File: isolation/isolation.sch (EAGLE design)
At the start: 37 parts, among them IC1 XTLV61048DBVR, IC2 SN74HC14DRG3, IC3 SN74HCS32PWR, IC4 SN74HCS08DYYR, J1 S4B-XH-A_LF__SN_, J2 S4B-XH-A_LF__SN_

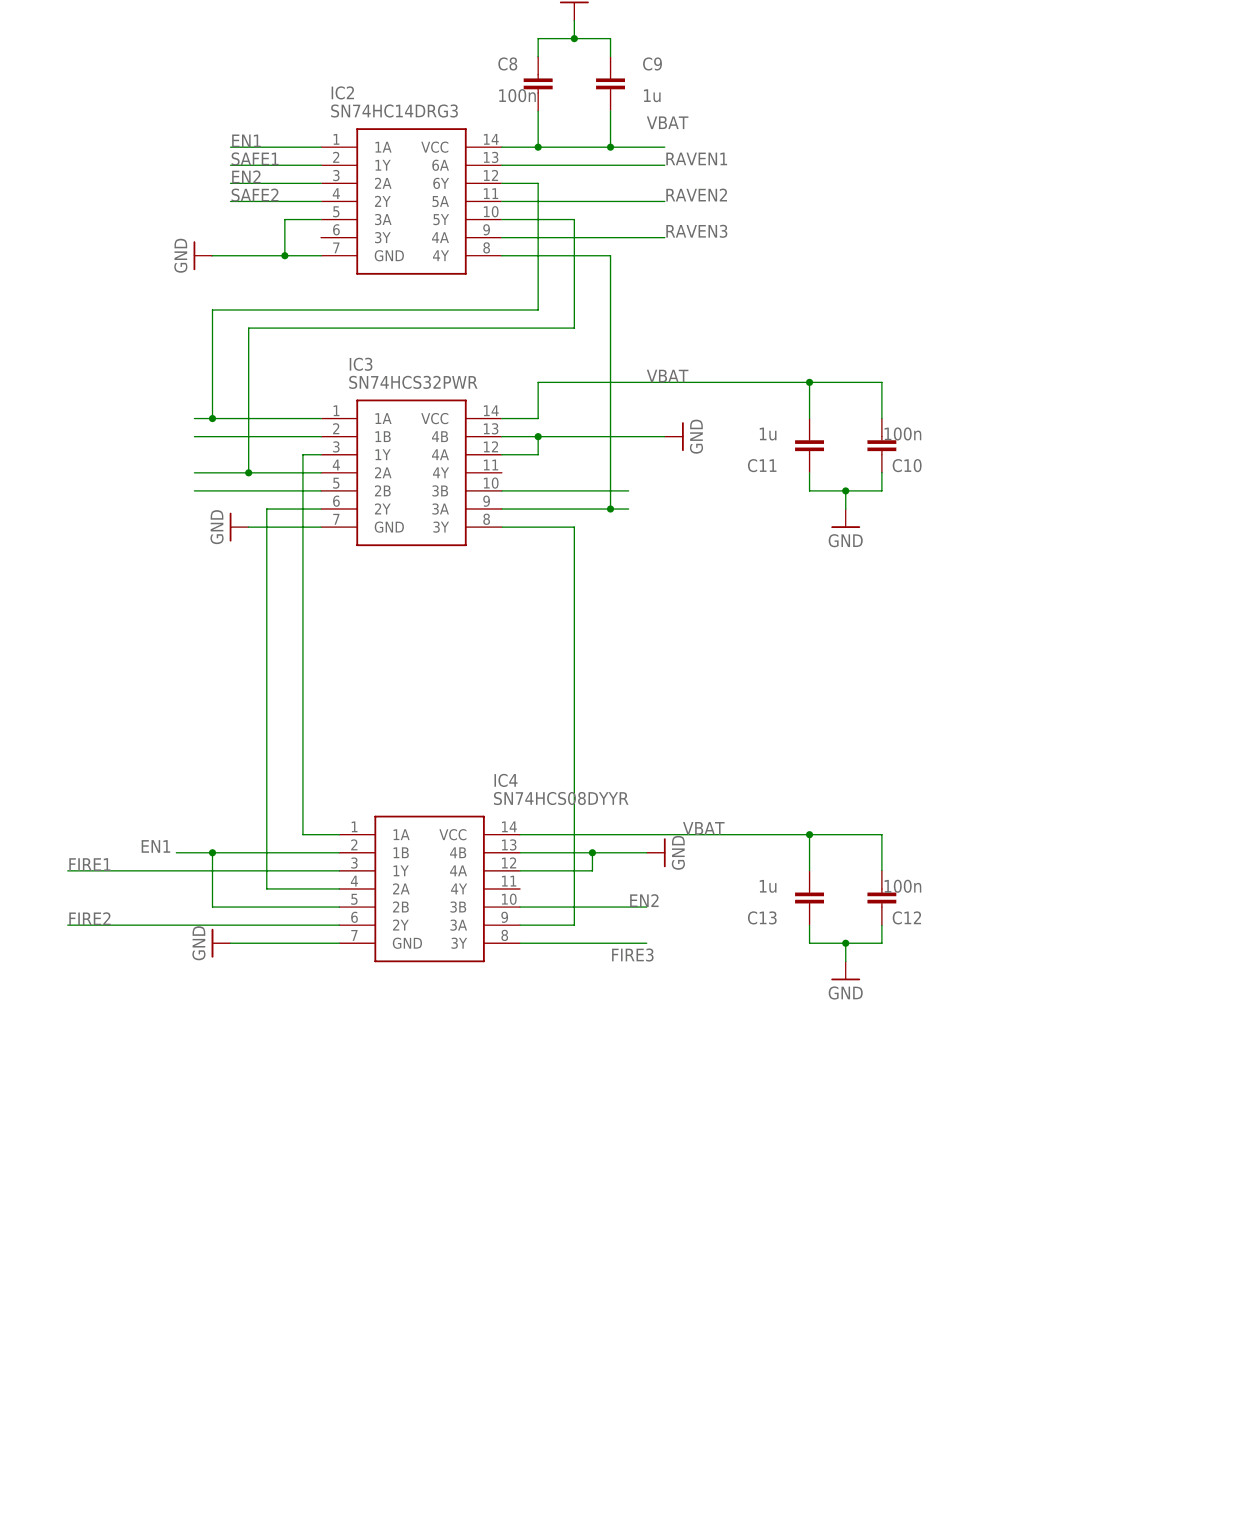
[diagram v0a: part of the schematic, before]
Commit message: fire control mosfet
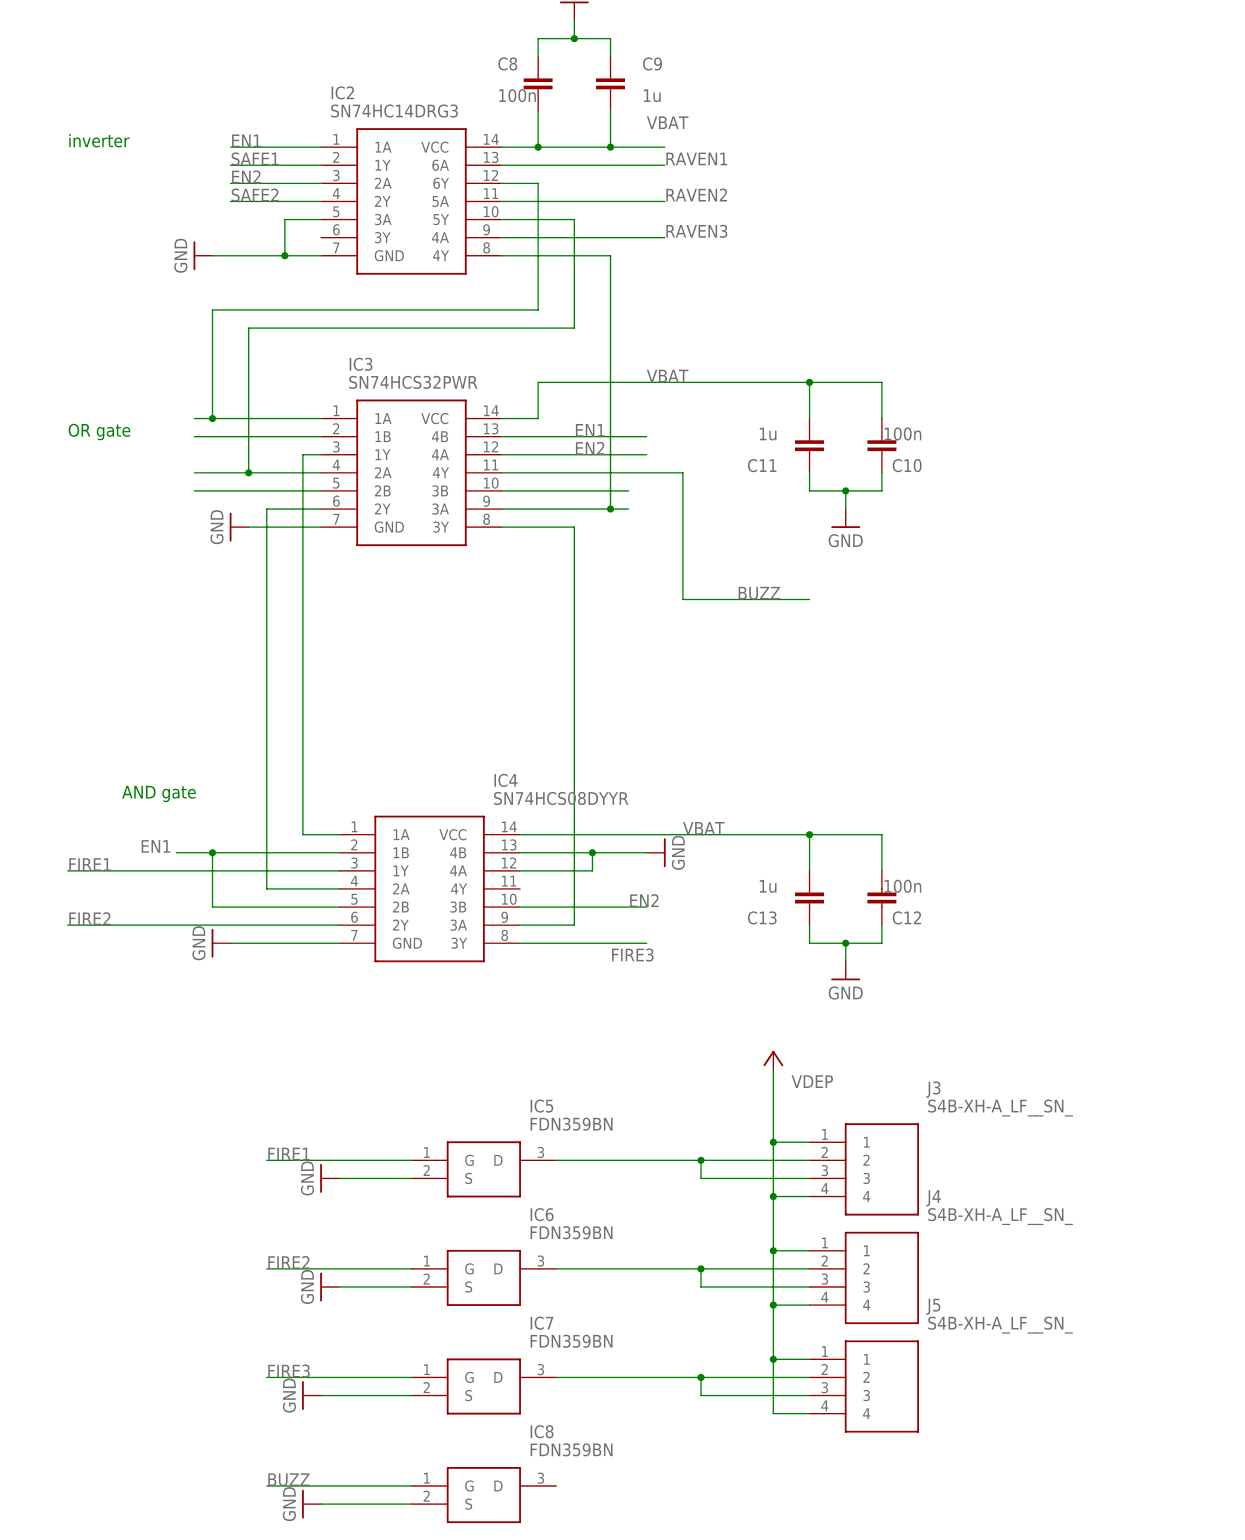
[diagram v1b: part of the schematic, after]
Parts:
- added IC5, IC6, IC7, IC8: FDN359BN, SamacSys_Parts:FDN359BN
- added J3, J4, J5: S4B-XH-A_LF__SN_, SamacSys_Parts:S4B-XH-A_LF__SN_
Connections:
- new net BUZZ: IC3.4Y, IC8.G
- new net N$17: IC5.D, J3.2, J3.3
- new net N$19: IC6.D, J4.2, J4.3
- new net N$20: IC7.D, J5.2, J5.3
- net EN1: now also IC3.4B
- net EN2: now also IC3.4A
- net FIRE1: now also IC5.G
- net FIRE2: now also IC6.G
- net FIRE3: now also IC7.G
- net GND: now also IC5.S, IC6.S, IC7.S, IC8.S; no longer IC3.4A, IC3.4B
- net VDEP: now also J3.1, J3.4, J4.1, J4.4, J5.1, J5.4
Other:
- note added: "AND gate"
- note added: "OR gate"
- note added: "inverter"

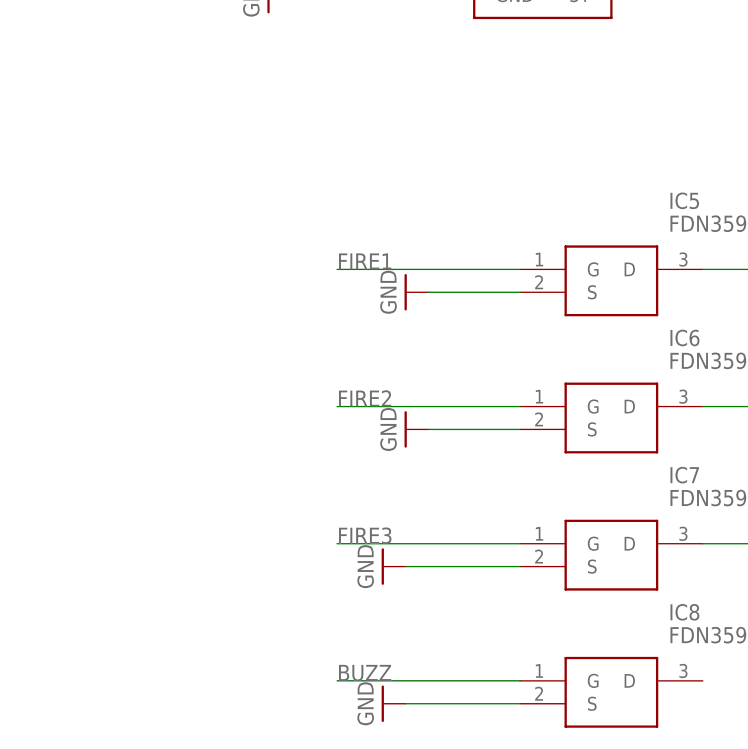
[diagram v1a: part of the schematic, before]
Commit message: pull down resistors on mosfets
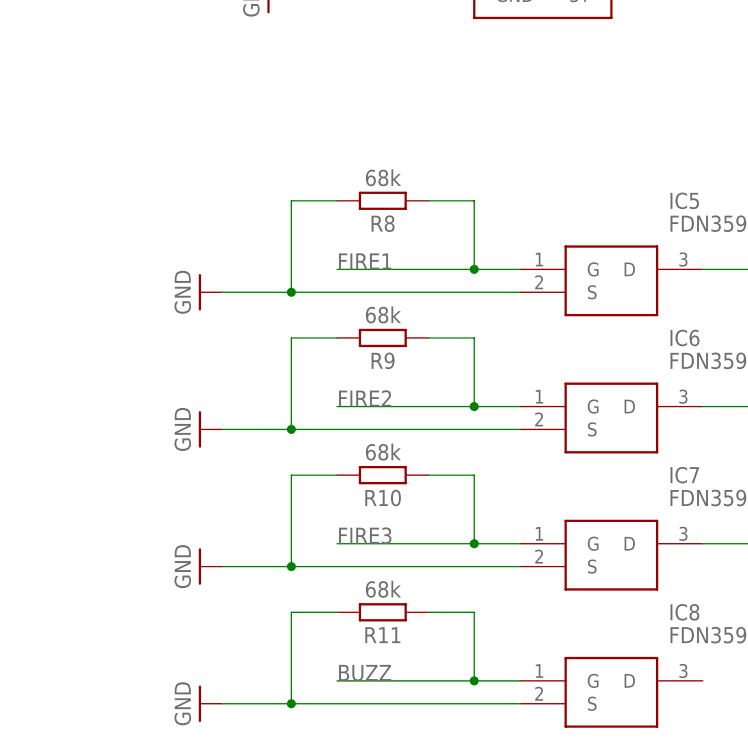
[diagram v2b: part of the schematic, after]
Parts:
- added R10, R11, R8, R9: 68k, Resistor:R_CHIP-0603(1608-METRIC)
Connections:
- net BUZZ: now also R11.1
- net FIRE1: now also R8.1
- net FIRE2: now also R9.1
- net FIRE3: now also R10.1
- net GND: now also R10.2, R11.2, R8.2, R9.2
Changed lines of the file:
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@@
 <part name="J5" library="SamacSys_Parts" deviceset="S4B-XH-A_LF__SN_" device=""/>
 <part name="P+1" library="supply1" library_urn="urn:adsk.eagle:library:371" deviceset="VCC" device=""/>
+<part name="R8" library="Resistor" library_urn="urn:adsk.eagle:library:16378527" deviceset="R" device="CHIP-0603(1608-METRIC)" package3d_urn="urn:adsk.eagle:package:16378565/5" technology="_" value="68k"/>
+<part name="R9" library="Resistor" library_urn="urn:adsk.eagle:library:16378527" deviceset="R" device="CHIP-0603(1608-METRIC)" package3d_urn="urn:adsk.eagle:package:16378565/5" technology="_" value="68k"/>
+<part name="R10" library="Resistor" library_urn="urn:adsk.eagle:library:16378527" deviceset="R" device="CHIP-0603(1608-METRIC)" package3d_urn="urn:adsk.eagle:package:16378565/5" technology="_" value="68k"/>
+<part name="R11" library="Resistor" library_urn="urn:adsk.eagle:library:16378527" deviceset="R" device="CHIP-0603(1608-METRIC)" package3d_urn="urn:adsk.eagle:package:16378565/5" technology="_" value="68k"/>
 </parts>
 <sheets>
@@
 <attribute name="VALUE" x="52.07" y="-332.74" size="1.778" layer="96" align="center-left"/>
 </instance>
-<instance part="SUPPLY17" gate="G$1" x="22.86" y="-294.64" smashed="yes" rot="R270">
-<attribute name="VALUE" x="20.955" y="-294.64" size="1.778" layer="96" rot="R270" align="center"/>
-</instance>
-<instance part="SUPPLY21" gate="G$1" x="22.86" y="-309.88" smashed="yes" rot="R270">
-<attribute name="VALUE" x="20.955" y="-309.88" size="1.778" layer="96" rot="R270" align="center"/>
-</instance>
-<instance part="SUPPLY22" gate="G$1" x="20.32" y="-325.12" smashed="yes" rot="R270">
-<attribute name="VALUE" x="18.415" y="-325.12" size="1.778" layer="96" rot="R270" align="center"/>
-</instance>
-<instance part="SUPPLY23" gate="G$1" x="20.32" y="-340.36" smashed="yes" rot="R270">
-<attribute name="VALUE" x="18.415" y="-340.36" size="1.778" layer="96" rot="R270" align="center"/>
+<instance part="SUPPLY17" gate="G$1" x="0" y="-294.64" smashed="yes" rot="R270">
+<attribute name="VALUE" x="-1.905" y="-294.64" size="1.778" layer="96" rot="R270" align="center"/>
+</instance>
+<instance part="SUPPLY21" gate="G$1" x="0" y="-309.88" smashed="yes" rot="R270">
+<attribute name="VALUE" x="-1.905" y="-309.88" size="1.778" layer="96" rot="R270" align="center"/>
+</instance>
+<instance part="SUPPLY22" gate="G$1" x="0" y="-325.12" smashed="yes" rot="R270">
+<attribute name="VALUE" x="-1.905" y="-325.12" size="1.778" layer="96" rot="R270" align="center"/>
+</instance>
+<instance part="SUPPLY23" gate="G$1" x="0" y="-340.36" smashed="yes" rot="R270">
+<attribute name="VALUE" x="-1.905" y="-340.36" size="1.778" layer="96" rot="R270" align="center"/>
 </instance>
 <instance part="J3" gate="G$1" x="91.44" y="-289.56" smashed="yes">
@@
 </instance>
 <instance part="P+1" gate="VCC" x="86.36" y="-276.86" smashed="yes"/>
+<instance part="R8" gate="G$1" x="20.32" y="-284.48" smashed="yes" rot="R180">
+<attribute name="NAME" x="20.32" y="-287.02" size="1.778" layer="95" rot="R180" align="center"/>
+<attribute name="VALUE" x="20.32" y="-281.94" size="1.778" layer="96" rot="R180" align="center"/>
+</instance>
+<instance part="R9" gate="G$1" x="20.32" y="-299.72" smashed="yes" rot="R180">
+<attribute name="NAME" x="20.32" y="-302.26" size="1.778" layer="95" rot="R180" align="center"/>
+<attribute name="VALUE" x="20.32" y="-297.18" size="1.778" layer="96" rot="R180" align="center"/>
+</instance>
+<instance part="R10" gate="G$1" x="20.32" y="-314.96" smashed="yes" rot="R180">
+<attribute name="NAME" x="20.32" y="-317.5" size="1.778" layer="95" rot="R180" align="center"/>
+<attribute name="VALUE" x="20.32" y="-312.42" size="1.778" layer="96" rot="R180" align="center"/>
+</instance>
+<instance part="R11" gate="G$1" x="20.32" y="-330.2" smashed="yes" rot="R180">
+<attribute name="NAME" x="20.32" y="-332.74" size="1.778" layer="95" rot="R180" align="center"/>
+<attribute name="VALUE" x="20.32" y="-327.66" size="1.778" layer="96" rot="R180" align="center"/>
+</instance>
 </instances>
 <busses>
@@
 <pinref part="IC5" gate="G$1" pin="S"/>
 <pinref part="SUPPLY17" gate="G$1" pin="GND"/>
-<wire x1="35.56" y1="-294.64" x2="25.4" y2="-294.64" width="0.1524" layer="91"/>
+<wire x1="35.56" y1="-294.64" x2="10.16" y2="-294.64" width="0.1524" layer="91"/>
+<pinref part="R8" gate="G$1" pin="2"/>
+<wire x1="10.16" y1="-294.64" x2="2.54" y2="-294.64" width="0.1524" layer="91"/>
+<wire x1="15.24" y1="-284.48" x2="10.16" y2="-284.48" width="0.1524" layer="91"/>
+<wire x1="10.16" y1="-284.48" x2="10.16" y2="-294.64" width="0.1524" layer="91"/>
+<junction x="10.16" y="-294.64"/>
 </segment>
 <segment>
 <pinref part="IC6" gate="G$1" pin="S"/>
 <pinref part="SUPPLY21" gate="G$1" pin="GND"/>
-<wire x1="35.56" y1="-309.88" x2="25.4" y2="-309.88" width="0.1524" layer="91"/>
+<wire x1="35.56" y1="-309.88" x2="10.16" y2="-309.88" width="0.1524" layer="91"/>
+<pinref part="R9" gate="G$1" pin="2"/>
+<wire x1="10.16" y1="-309.88" x2="2.54" y2="-309.88" width="0.1524" layer="91"/>
+<wire x1="15.24" y1="-299.72" x2="10.16" y2="-299.72" width="0.1524" layer="91"/>
+<wire x1="10.16" y1="-299.72" x2="10.16" y2="-309.88" width="0.1524" layer="91"/>
+<junction x="10.16" y="-309.88"/>
 </segment>
 <segment>
 <pinref part="IC7" gate="G$1" pin="S"/>
 <pinref part="SUPPLY22" gate="G$1" pin="GND"/>
-<wire x1="35.56" y1="-325.12" x2="22.86" y2="-325.12" width="0.1524" layer="91"/>
+<wire x1="35.56" y1="-325.12" x2="10.16" y2="-325.12" width="0.1524" layer="91"/>
+<pinref part="R10" gate="G$1" pin="2"/>
+<wire x1="10.16" y1="-325.12" x2="2.54" y2="-325.12" width="0.1524" layer="91"/>
+<wire x1="15.24" y1="-314.96" x2="10.16" y2="-314.96" width="0.1524" layer="91"/>
+<wire x1="10.16" y1="-314.96" x2="10.16" y2="-325.12" width="0.1524" layer="91"/>
+<junction x="10.16" y="-325.12"/>
 </segment>
 <segment>
 <pinref part="IC8" gate="G$1" pin="S"/>
 <pinref part="SUPPLY23" gate="G$1" pin="GND"/>
-<wire x1="35.56" y1="-340.36" x2="22.86" y2="-340.36" width="0.1524" layer="91"/>
+<wire x1="35.56" y1="-340.36" x2="10.16" y2="-340.36" width="0.1524" layer="91"/>
+<pinref part="R11" gate="G$1" pin="2"/>
+<wire x1="10.16" y1="-340.36" x2="2.54" y2="-340.36" width="0.1524" layer="91"/>
+<wire x1="15.24" y1="-330.2" x2="10.16" y2="-330.2" width="0.1524" layer="91"/>
+<wire x1="10.16" y1="-330.2" x2="10.16" y2="-340.36" width="0.1524" layer="91"/>
+<junction x="10.16" y="-340.36"/>
 </segment>
 </net>
@@
 <segment>
 <pinref part="IC5" gate="G$1" pin="G"/>
-<wire x1="35.56" y1="-292.1" x2="15.24" y2="-292.1" width="0.1524" layer="91"/>
+<wire x1="35.56" y1="-292.1" x2="30.48" y2="-292.1" width="0.1524" layer="91"/>
 <label x="15.24" y="-292.1" size="1.778" layer="95"/>
+<pinref part="R8" gate="G$1" pin="1"/>
+<wire x1="30.48" y1="-292.1" x2="15.24" y2="-292.1" width="0.1524" layer="91"/>
+<wire x1="25.4" y1="-284.48" x2="30.48" y2="-284.48" width="0.1524" layer="91"/>
+<wire x1="30.48" y1="-284.48" x2="30.48" y2="-292.1" width="0.1524" layer="91"/>
+<junction x="30.48" y="-292.1"/>
 </segment>
 </net>
@@
 <segment>
 <pinref part="IC6" gate="G$1" pin="G"/>
-<wire x1="35.56" y1="-307.34" x2="15.24" y2="-307.34" width="0.1524" layer="91"/>
+<wire x1="35.56" y1="-307.34" x2="30.48" y2="-307.34" width="0.1524" layer="91"/>
 <label x="15.24" y="-307.34" size="1.778" layer="95"/>
+<pinref part="R9" gate="G$1" pin="1"/>
+<wire x1="30.48" y1="-307.34" x2="15.24" y2="-307.34" width="0.1524" layer="91"/>
+<wire x1="25.4" y1="-299.72" x2="30.48" y2="-299.72" width="0.1524" layer="91"/>
+<wire x1="30.48" y1="-299.72" x2="30.48" y2="-307.34" width="0.1524" layer="91"/>
+<junction x="30.48" y="-307.34"/>
 </segment>
 </net>
@@
 <segment>
 <pinref part="IC7" gate="G$1" pin="G"/>
-<wire x1="35.56" y1="-322.58" x2="15.24" y2="-322.58" width="0.1524" layer="91"/>
+<wire x1="35.56" y1="-322.58" x2="30.48" y2="-322.58" width="0.1524" layer="91"/>
 <label x="15.24" y="-322.58" size="1.778" layer="95"/>
+<pinref part="R10" gate="G$1" pin="1"/>
+<wire x1="30.48" y1="-322.58" x2="15.24" y2="-322.58" width="0.1524" layer="91"/>
+<wire x1="25.4" y1="-314.96" x2="30.48" y2="-314.96" width="0.1524" layer="91"/>
+<wire x1="30.48" y1="-314.96" x2="30.48" y2="-322.58" width="0.1524" layer="91"/>
+<junction x="30.48" y="-322.58"/>
 </segment>
 </net>
@@
 <segment>
 <pinref part="IC8" gate="G$1" pin="G"/>
-<wire x1="35.56" y1="-337.82" x2="15.24" y2="-337.82" width="0.1524" layer="91"/>
+<wire x1="35.56" y1="-337.82" x2="30.48" y2="-337.82" width="0.1524" layer="91"/>
 <label x="15.24" y="-337.82" size="1.778" layer="95"/>
-</segment>
-</net>
+<pinref part="R11" gate="G$1" pin="1"/>
+<wire x1="30.48" y1="-337.82" x2="15.24" y2="-337.82" width="0.1524" layer="91"/>
+<wire x1="25.4" y1="-330.2" x2="30.48" y2="-330.2" width="0.1524" layer="91"/>
+<wire x1="30.48" y1="-330.2" x2="30.48" y2="-337.82" width="0.1524" layer="91"/>
+<junction x="30.48" y="-337.82"/>
+</segment>
+</net>

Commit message: danger buzzer
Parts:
- added LS1: CMI-9705-85-SMT-TR, SamacSys_Parts:CMI-9705-85-SMT-TR
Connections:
- new net N$22: IC8.D, LS1.-
- net VDEP: now also LS1.+
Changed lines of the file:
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@@
 <part name="R10" library="Resistor" library_urn="urn:adsk.eagle:library:16378527" deviceset="R" device="CHIP-0603(1608-METRIC)" package3d_urn="urn:adsk.eagle:package:16378565/5" technology="_" value="68k"/>
 <part name="R11" library="Resistor" library_urn="urn:adsk.eagle:library:16378527" deviceset="R" device="CHIP-0603(1608-METRIC)" package3d_urn="urn:adsk.eagle:package:16378565/5" technology="_" value="68k"/>
+<part name="LS1" library="SamacSys_Parts" deviceset="CMI-9705-85-SMT-TR" device=""/>
 </parts>
 <sheets>
@@
 <attribute name="NAME" x="20.32" y="-332.74" size="1.778" layer="95" rot="R180" align="center"/>
 <attribute name="VALUE" x="20.32" y="-327.66" size="1.778" layer="96" rot="R180" align="center"/>
+</instance>
+<instance part="LS1" gate="G$1" x="93.98" y="-337.82" smashed="yes">
+<attribute name="NAME" x="105.41" y="-337.82" size="1.778" layer="95" align="center-left"/>
+<attribute name="VALUE" x="105.41" y="-340.36" size="1.778" layer="96" align="center-left"/>
 </instance>
 </instances>
@@
 <junction x="86.36" y="-289.56"/>
 <label x="88.9" y="-281.94" size="1.778" layer="95"/>
+<pinref part="LS1" gate="G$1" pin="+"/>
+<wire x1="93.98" y1="-337.82" x2="86.36" y2="-337.82" width="0.1524" layer="91"/>
+<wire x1="86.36" y1="-337.82" x2="86.36" y2="-327.66" width="0.1524" layer="91"/>
+<junction x="86.36" y="-327.66"/>
 </segment>
 </net>
@@
 </segment>
 </net>
+<net name="N$22" class="0">
+<segment>
+<pinref part="LS1" gate="G$1" pin="-"/>
+<wire x1="93.98" y1="-340.36" x2="93.98" y2="-342.9" width="0.1524" layer="91"/>
+<wire x1="93.98" y1="-342.9" x2="60.96" y2="-342.9" width="0.1524" layer="91"/>
+<wire x1="60.96" y1="-342.9" x2="60.96" y2="-337.82" width="0.1524" layer="91"/>
+<pinref part="IC8" gate="G$1" pin="D"/>
+<wire x1="60.96" y1="-337.82" x2="55.88" y2="-337.82" width="0.1524" layer="91"/>
+</segment>
+</net>

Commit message: usb c power
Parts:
- added C14: 100n, Capacitor:C_CHIP-0603(1608-METRIC)
- added C15: 1u, Capacitor:C_CHIP-0603(1608-METRIC)
- added D2, D3, D4: (no value), adafruit:DIODE_SOD-123FL
- added J6: (no value), SparkFun-Connectors:USB_C_2-LAYER_PADS
- added R12, R14: 5k1, Resistor:R_CHIP-0603(1608-METRIC)
- added R13: 1M, Resistor:R_CHIP-0603(1608-METRIC)
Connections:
- new net N$21: J6.SHLD, R13.1
- new net N$24: J6.CC2, R12.1
- new net N$25: J6.CC1, R14.1
- new net N$26: C14.2, C15.2, D2.A, D3.A, D4.A, J6.VBUS
- net GND: now also C14.1, C15.1, J6.GND, R12.2, R13.2, R14.2
- net VBAT: now also D2.C, D3.C, D4.C
